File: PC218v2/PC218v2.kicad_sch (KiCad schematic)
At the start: 49 parts, among them J1 PC218_BoardEdge_44pin, Q1 BC848W, Q10 BC848W, Q11 BC848W, Q12 BC848W, Q13 BC848W, Q14 BC848W, Q15 BC848W, Q2 BC848W, Q3 BC848W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

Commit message: Rename project files for PC218 Rev 2
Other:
- company: (none) -> Peter Farley
- title: (none) -> Keithley 615 PC218 Replacement v2
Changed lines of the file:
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@@
 (kicad_sch (version 20211123) (generator eeschema)
-  (paper "A3")
+  (paper "USLegal")
+  (title_block
+    (title "Keithley 615 PC218 Replacement v2")
+    (rev "1.0")
+    (company "Peter Farley")
+  )
   (junction (at 298.45 127) (diameter 0) (color 0 0 0 0)
   )

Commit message: PC218 Rev 2.1
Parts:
- J1: footprint keithley_615_part_library:PC218_Edge_Connector -> footprints:PC218_Edge_Connector; symbol keithley_615_sym_library:PC218_BoardEdge_44pin -> lib_symbols:PC218_BoardEdge_44pin
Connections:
- no-connect marks 0 -> 4
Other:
- title: Keithley 615 PC218 Replacement v2 -> Keithley 615 PC218 Replacement Board
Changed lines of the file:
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@@
   (paper "USLegal")
   (title_block
-    (title "Keithley 615 PC218 Replacement v2")
-    (rev "1.0")
+    (title "Keithley 615 PC218 Replacement Board")
+    (date "2023-01-10")
+    (rev "2.0")
     (company "Peter Farley")
+    (comment 1 "Rev 1: Initial design")
   )
   (junction (at 298.45 127) (diameter 0) (color 0 0 0 0)
@@
   (junction (at 326.39 111.76) (diameter 0) (color 0 0 0 0)
   )
+  (no_connect (at 275.59 26.67))
+  (no_connect (at 284.48 125.73))
+  (no_connect (at 284.48 111.76))
+  (no_connect (at 284.48 97.79))
   (wire (pts (xy 102.87 40.64) (xy 102.87 41.91))
     (stroke (width 0) (type default) (color 0 0 0 0))
@@
     (pin "2")
   )
-  (symbol (lib_id "keithley_615_sym_library:PC218_BoardEdge_44pin") (at 292.1 24.13 0) (unit 1)
+  (symbol (lib_id "lib_symbols:PC218_BoardEdge_44pin") (at 292.1 24.13 0) (unit 1)
     (in_bom yes) (on_board yes) (fields_autoplaced)
     (property "Reference" "J1" (id 0) (at 291.465 20.32 0))
     (property "Value" "PC218_BoardEdge_44pin" (id 1) (at 291.465 22.86 0))
-    (property "Footprint" "keithley_615_part_library:PC218_Edge_Connector" (id 2) (at 290.83 24.13 0)
+    (property "Footprint" "footprints:PC218_Edge_Connector" (id 2) (at 290.83 24.13 0)
       (effects (font (size 1.27 1.27)) hide)
     )
@@
     )
     (path "/0b3e7a7c-ceb5-44cc-8e1c-4b20ca10ed23"
-      (reference "J1") (unit 1) (value "PC218_BoardEdge_44pin") (footprint "keithley_615_part_library:PC218_Edge_Connector")
+      (reference "J1") (unit 1) (value "PC218_BoardEdge_44pin") (footprint "footprints:PC218_Edge_Connector")
     )
     (path "/4446f63d-df20-417e-add3-680a46456664"

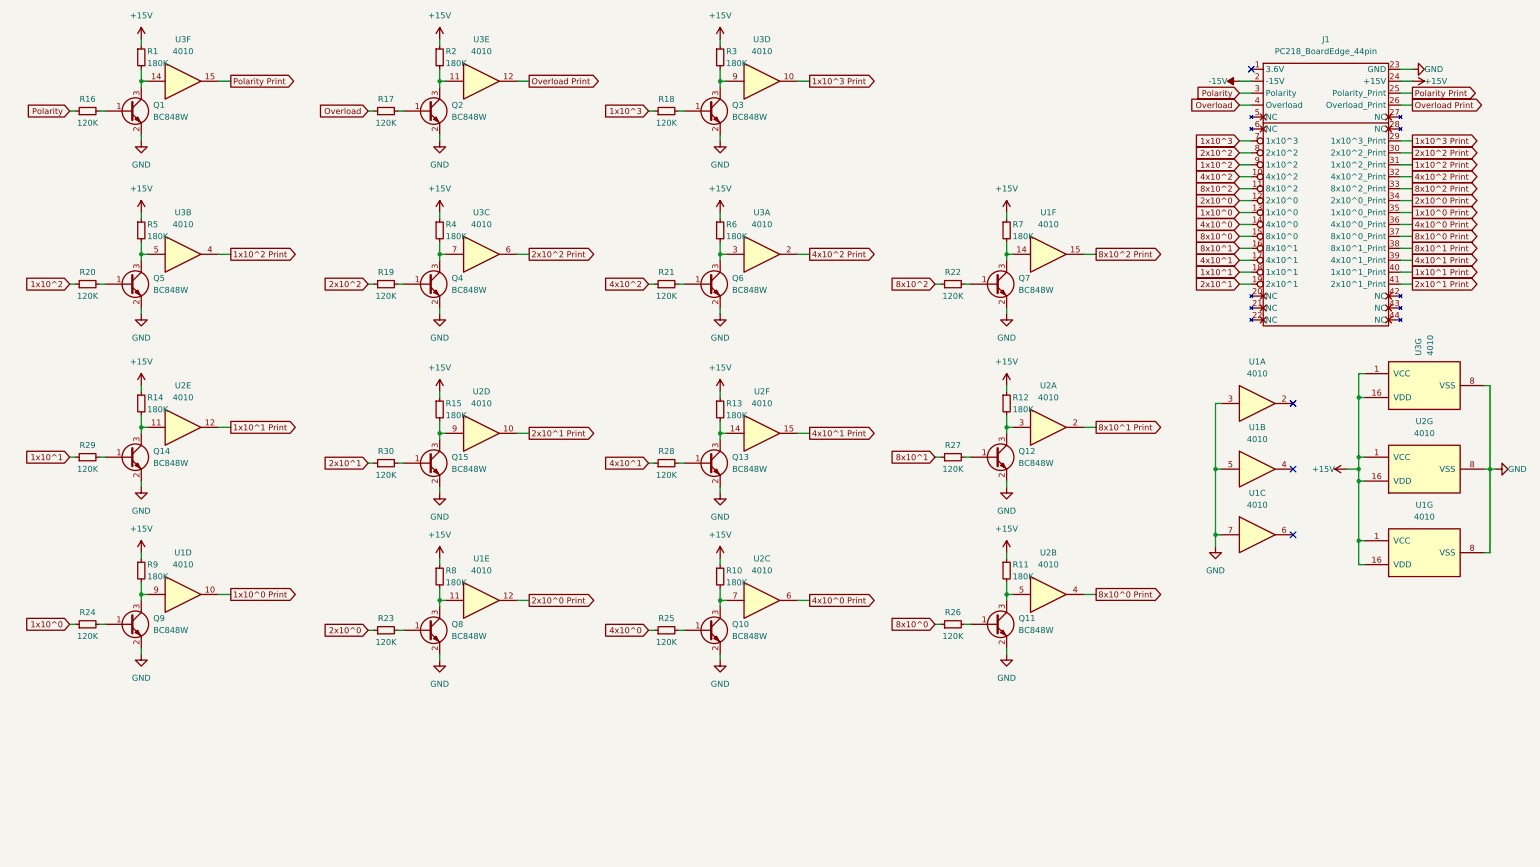
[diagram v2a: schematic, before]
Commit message: PC218v2: Rev 2.2
Matched form factor of new PC209 board
Added power test points
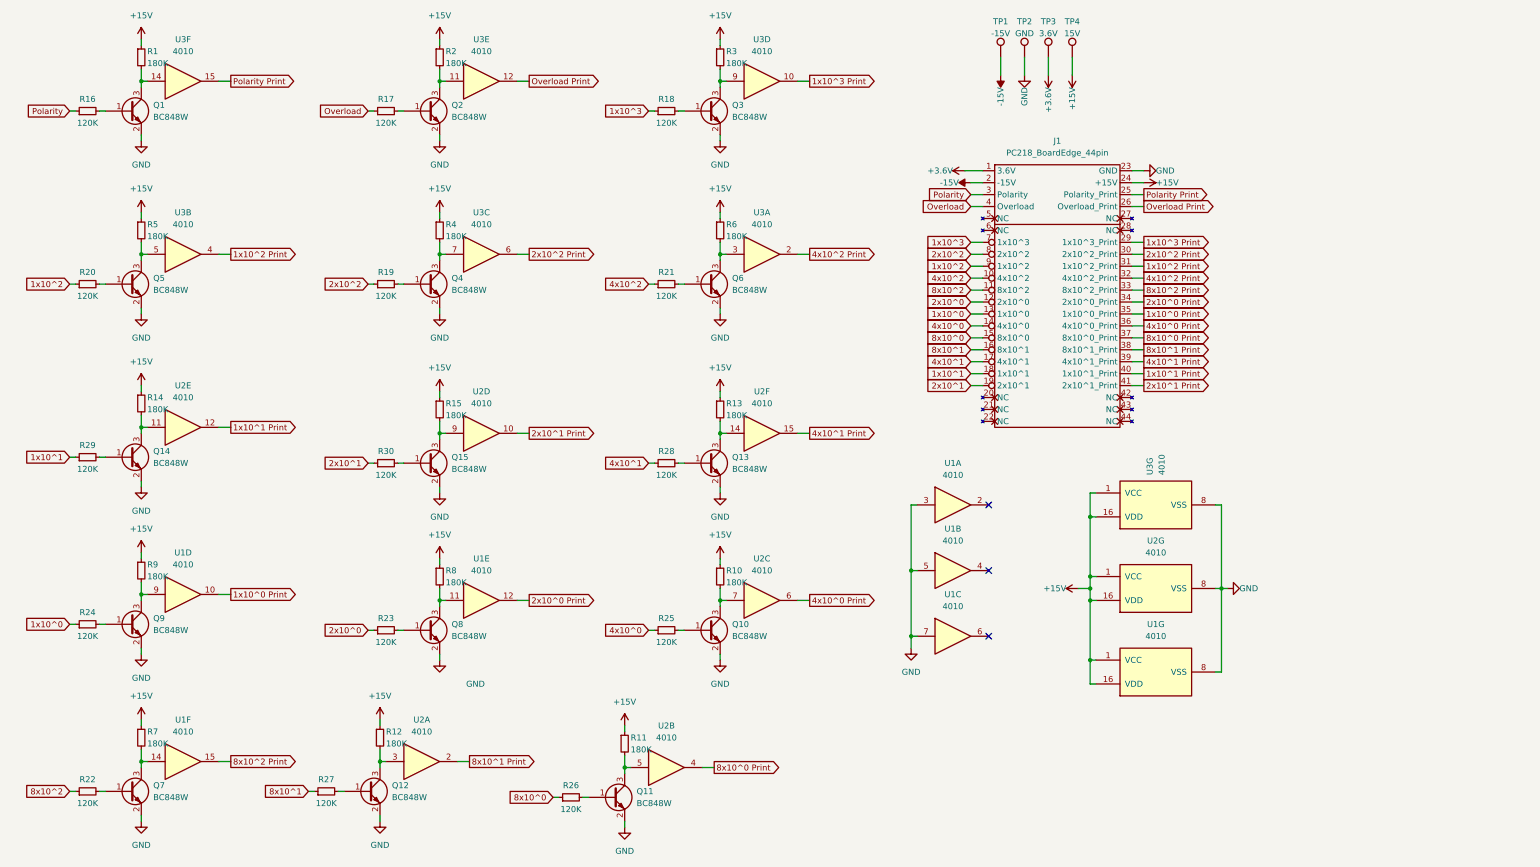
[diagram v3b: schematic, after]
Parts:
- added TP1: -15V, TestPoint:TestPoint_THTPad_2.0x2.0mm_Drill1.0mm, symbol Connector:TestPoint
- added TP2: GND, TestPoint:TestPoint_THTPad_2.0x2.0mm_Drill1.0mm, symbol Connector:TestPoint
- added TP3: 3.6V, TestPoint:TestPoint_THTPad_2.0x2.0mm_Drill1.0mm, symbol Connector:TestPoint
- added TP4: 15V, TestPoint:TestPoint_THTPad_2.0x2.0mm_Drill1.0mm, symbol Connector:TestPoint
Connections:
- net +15V: now also TP4.1
- net -15V: now also TP1.1
- net GND: now also TP2.1
- net +3.6V: now reaches J1.1 (3.6V)
- net +3.6V: now also TP3.1
- no-connect marks 4 -> 3
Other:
- moved on the sheet: J1, Q11, Q12, Q7, R11, R12, R22, R26, R27, R7, U1A, U1B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
